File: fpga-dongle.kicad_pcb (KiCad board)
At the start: 2 copper layers, 85.8 x 137 mm, 109 parts, among them P1 USB_PWR, P2 PGM, P3 right, P4 left, P5 CONN_01X40, P6 CONN_01X40, P7 DBG_SWD, P8 USB_PWR, Q1 BC857, SW1 T1107A(6x3,8x2,5MM)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

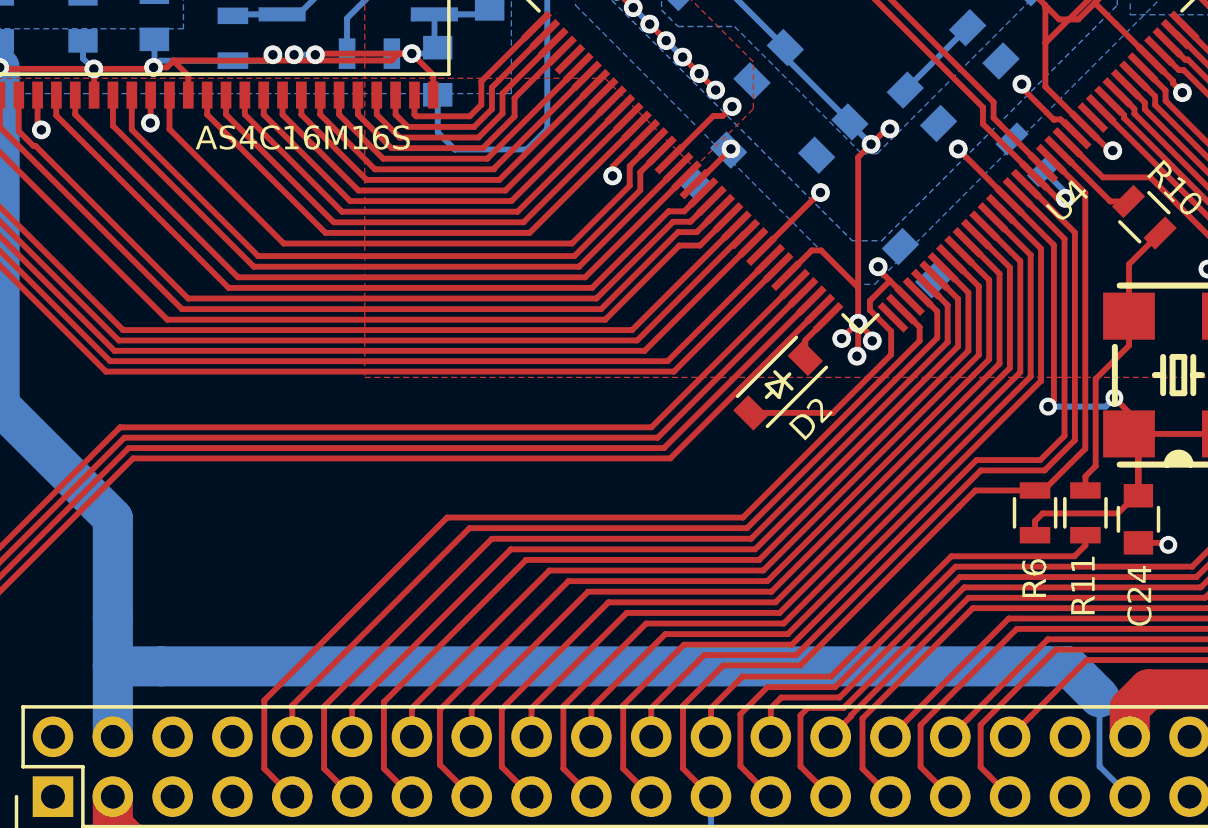
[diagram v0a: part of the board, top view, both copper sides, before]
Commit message: Fix 2V5 net diode from 1v2 to 3v3
Signed-off-by: Martin Ribelotta <martinribelotta@gmail.com>
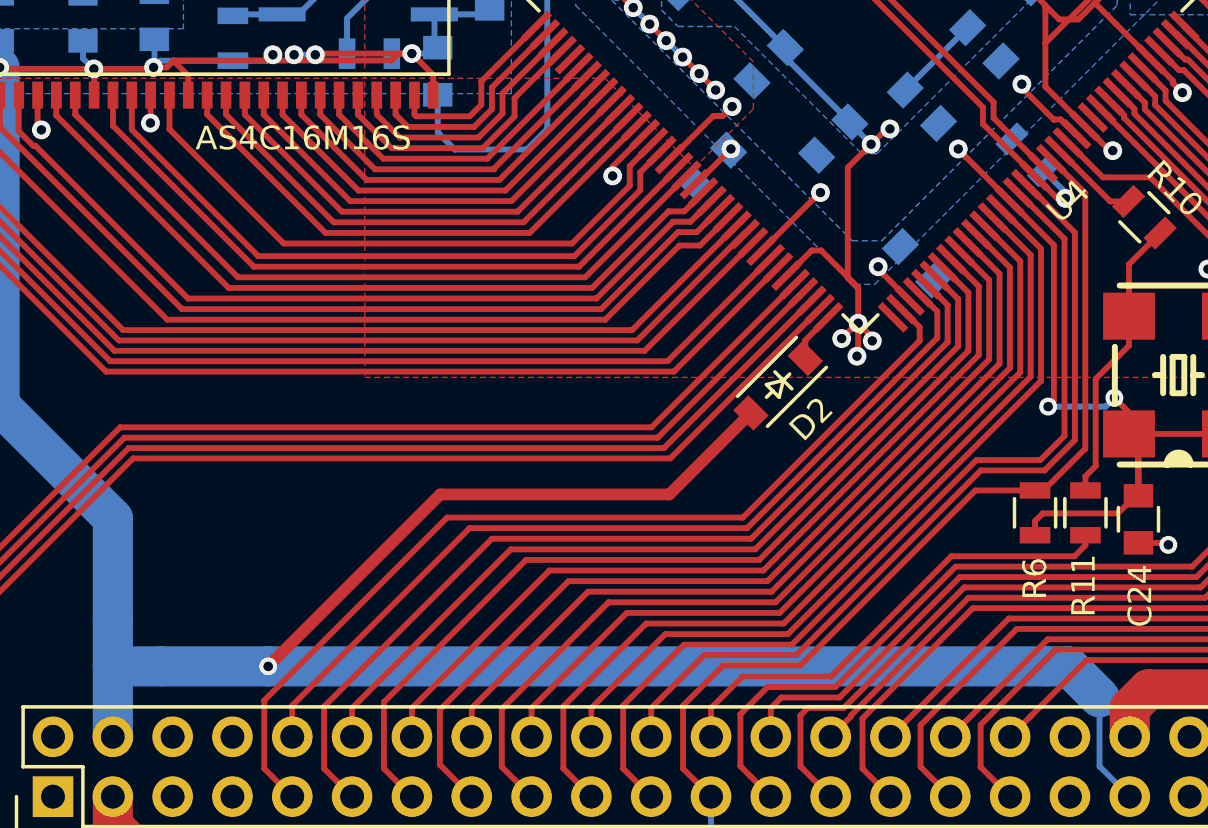
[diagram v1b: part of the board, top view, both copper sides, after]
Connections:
- D2 pad 2: +1V2 -> +3V3
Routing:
- net +3V3: track 528.2 -> 553.2 mm, vias 34 -> 35
- net +1V2: track 126.2 -> 115.3 mm
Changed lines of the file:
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@@
     (links 408)
     (no_connects 0)
-    (area 6.858 12.192 107.696001 163.068001)
+    (area 15.204999 17.544999 101.155001 154.695001)
     (thickness 1.6)
     (drawings 9)
@@
       (net 13 "Net-(D2-Pad1)"))
     (pad 2 smd rect (at 1.635 0 225) (size 0.91 1.22) (layers F.Cu F.Paste F.Mask)
-      (net 9 +1V2))
+      (net 1 +3V3))
   )
   (module OLIMEX_Devices-FP:FUSE-1206 (layer F.Cu)
@@
   (segment (start 81.802301 103.15) (end 81.743222 103.090921) (width 0.25) (layer B.Cu) (net 0))
   (via (at 81.743222 103.090921) (size 0.8) (drill 0.4) (layers F.Cu B.Cu) (net 0))
+  (segment (start 63.89388 124.90612) (end 60.43 128.37) (width 0.5) (layer F.Cu) (net 1))
+  (segment (start 60.43 128.37) (end 50.7 128.37) (width 0.5) (layer F.Cu) (net 1))
+  (segment (start 50.7 128.37) (end 43.4 135.67) (width 0.5) (layer F.Cu) (net 1))
+  (segment (start 76.46 135.67) (end 43.4 135.67) (width 1.7) (layer B.Cu) (net 1))
+  (segment (start 43.4 135.67) (end 38.862266 135.67) (width 1.7) (layer B.Cu) (net 1))
+  (via (at 43.4 135.67) (size 0.762) (drill 0.4064) (layers F.Cu B.Cu) (net 1))
   (segment (start 22.11 81) (end 22.11 79.215) (width 1.7) (layer B.Cu) (net 1))
   (segment (start 22.11 79.215) (end 23.05 78.275) (width 1.7) (layer B.Cu) (net 1))
@@
   (segment (start 78.7 139.917566) (end 78.7 136.99) (width 0.25) (layer B.Cu) (net 1))
   (segment (start 77.38 135.67) (end 76.46 135.67) (width 1.7) (layer B.Cu) (net 1))
-  (segment (start 76.46 135.67) (end 38.862266 135.67) (width 1.7) (layer B.Cu) (net 1))
   (segment (start 38.862266 135.67) (end 36.802266 135.67) (width 1.7) (layer B.Cu) (net 1))
   (segment (start 36.802266 135.67) (end 36.802266 138.659832) (width 1.7) (layer B.Cu) (net 1))
@@
   (segment (start 40.008666 110.588522) (end 39.365976 109.945832) (width 0.25) (layer F.Cu) (net 1))
   (segment (start 40.008666 111.413832) (end 40.008666 110.588522) (width 0.25) (layer F.Cu) (net 1) (status 10))
+  (segment (start 69 113.5) (end 68.01 114.49) (width 0.25) (layer F.Cu) (net 2))
+  (segment (start 68.01 114.49) (end 68.01 119.18) (width 0.25) (layer F.Cu) (net 2))
+  (segment (start 68.01 119.18) (end 68.45 119.62) (width 0.25) (layer F.Cu) (net 2))
   (segment (start 31.398213 48.16) (end 31.04 48.16) (width 0.25) (layer F.Cu) (net 2))
   (segment (start 32.108213 47.45) (end 31.398213 48.16) (width 0.25) (layer F.Cu) (net 2))
@@
   (segment (start 79.124071 113.77255) (end 79.260405 113.77255) (width 0.25) (layer F.Cu) (net 2))
   (via (at 79.260405 113.77255) (size 0.8) (drill 0.4) (layers F.Cu B.Cu) (net 2))
-  (segment (start 68.45 114.05) (end 68.45 119.62) (width 0.25) (layer F.Cu) (net 2))
   (segment (start 68.45 119.58) (end 68.45 119.62) (width 0.25) (layer F.Cu) (net 2))
   (segment (start 68.45 119.62) (end 68.45 121.1) (width 0.25) (layer F.Cu) (net 2))
@@
   (segment (start 69.65 112.85) (end 69 113.5) (width 0.25) (layer F.Cu) (net 2))
   (via (at 69.8 112.85) (size 0.8) (drill 0.4) (layers F.Cu B.Cu) (net 2))
-  (segment (start 69 113.5) (end 68.45 114.05) (width 0.25) (layer F.Cu) (net 2))
   (via (at 68.45 121.1) (size 0.8) (drill 0.4) (layers F.Cu B.Cu) (net 2))
   (segment (start 68.1 112.55) (end 68.1 112.6) (width 0.25) (layer B.Cu) (net 2) (status 30))
@@
   (segment (start 87.1 106.8) (end 81.05 106.8) (width 0.25) (layer B.Cu) (net 9))
   (segment (start 81.05 106.8) (end 71.95 97.7) (width 0.25) (layer B.Cu) (net 9))
-  (segment (start 68.949774 120.147947) (end 69.8 119.297721) (width 0.25) (layer F.Cu) (net 9))
-  (segment (start 63.89388 124.90612) (end 67.37924 124.90612) (width 0.25) (layer F.Cu) (net 9))
-  (segment (start 67.37924 124.90612) (end 69.85 122.43536) (width 0.25) (layer F.Cu) (net 9))
-  (segment (start 68.949774 120.541743) (end 68.949774 120.147947) (width 0.25) (layer F.Cu) (net 9))
-  (segment (start 69.85 121.441969) (end 68.949774 120.541743) (width 0.25) (layer F.Cu) (net 9))
-  (segment (start 69.85 122.43536) (end 69.85 121.441969) (width 0.25) (layer F.Cu) (net 9))
   (via (at 72.38 56.08) (size 0.762) (drill 0.4064) (layers F.Cu B.Cu) (net 9))
   (segment (start 72.38 55.3) (end 72.38 56.08) (width 1.2) (layer F.Cu) (net 9))

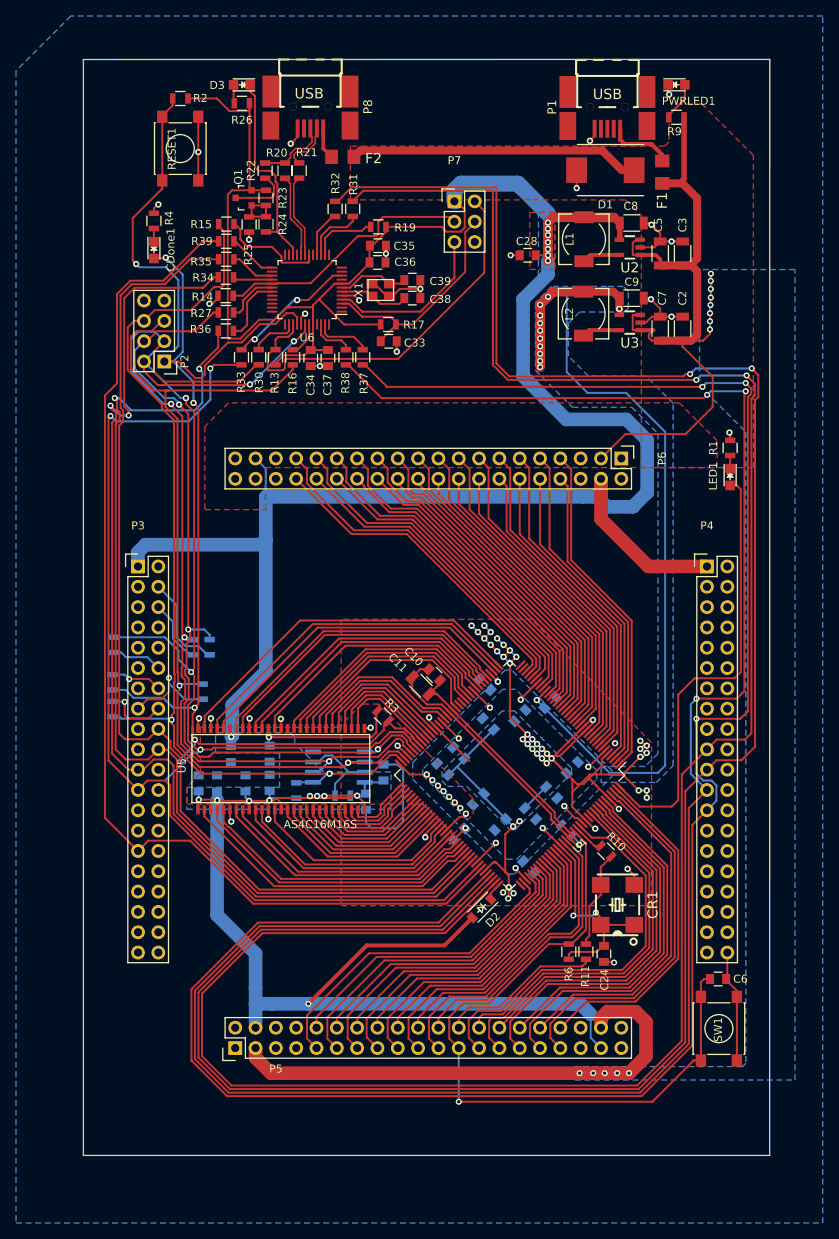
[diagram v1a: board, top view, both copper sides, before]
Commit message: Add miltiple power source handling, reroute pertinent nets
Signed-off-by: Martin Ribelotta <martinribelotta@gmail.com>
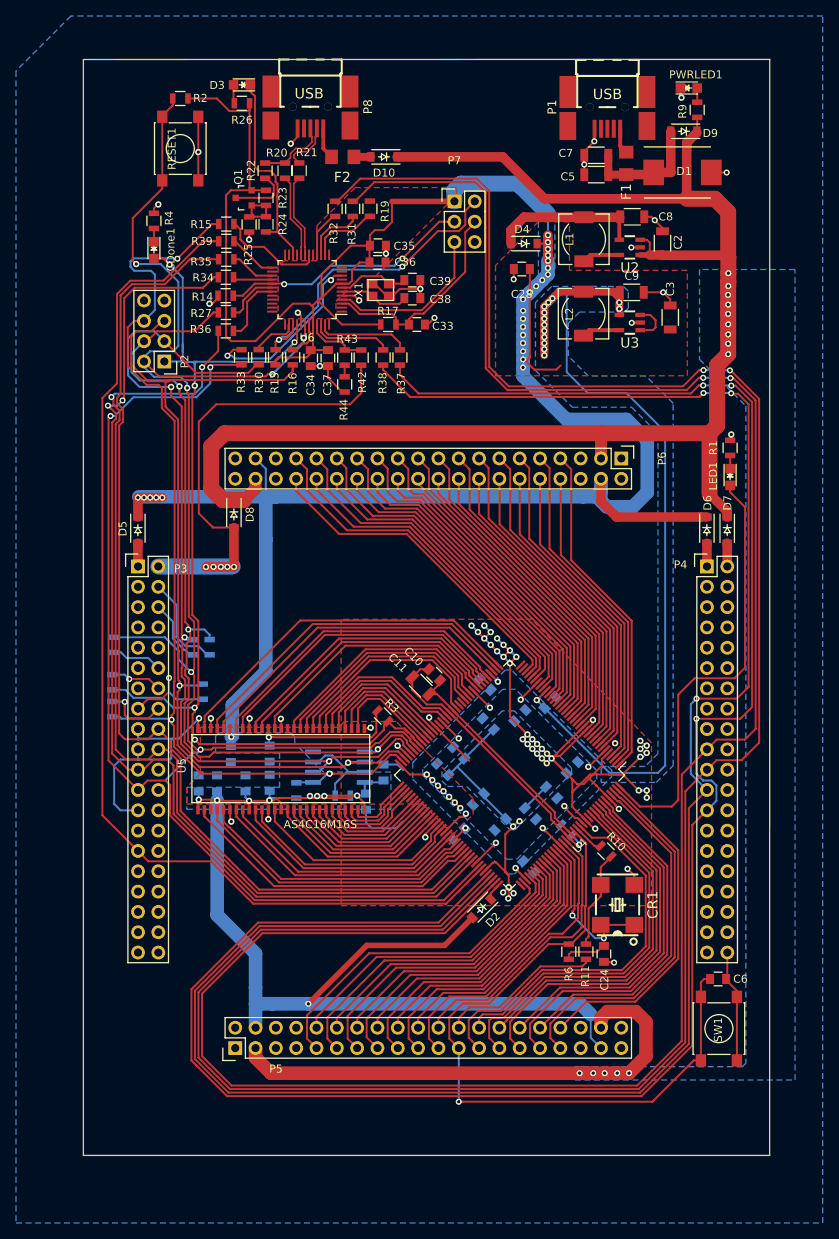
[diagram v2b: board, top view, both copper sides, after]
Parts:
- added D10: 1N5819(S4SOD-123), Diodes_SMD:SOD-123, F.Cu at (52.9, 29.8)
- added D4: 1N5819(S4SOD-123), Diodes_SMD:SOD-123, F.Cu at (70.4, 40.6)
- added D5: 1N5819(S4SOD-123), Diodes_SMD:SOD-123, F.Cu at (22.1, 76.5)
- added D6: 1N5819(S4SOD-123), Diodes_SMD:SOD-123, F.Cu at (93.2, 76.5)
- added D7: 1N5819(S4SOD-123), Diodes_SMD:SOD-123, F.Cu at (95.8, 76.5)
- added D8: 1N5819(S4SOD-123), Diodes_SMD:SOD-123, F.Cu at (34.1, 74.5)
- added D9: 1N5819(S4SOD-123), Diodes_SMD:SOD-123, F.Cu at (90.3, 26.6)
- added R42: 10k, Resistors_SMD:R_0805, F.Cu at (50.0, 54.9)
- added R43: 10k, Resistors_SMD:R_0805, F.Cu at (47.9, 54.9)
- added R44: 10k, Resistors_SMD:R_0805, F.Cu at (47.9, 58.2)
- moved C7 23.1 mm to (79.4, 29.6), turned to 0 degrees
- moved C5 12.7 mm to (79.4, 32.0), turned to 0 degrees
- moved C2 11.0 mm to (87.7, 40.6)
- moved D1 9.65 mm to (90.2, 31.8), turned to 0 degrees
- moved C3 8.14 mm to (88.6, 49.9)
- moved R37 4.65 mm to (54.9, 54.9)
- moved R38 4.65 mm to (52.8, 54.9)
- moved F1 4.63 mm to (83.1, 30.6)
- moved C33 4.09 mm to (57.0, 50.8)
- moved R9 2.76 mm to (92.0, 23.9), turned to 90 degrees
- moved R19 2.51 mm to (51.1, 36.3), turned to 90 degrees
- moved C28 1.87 mm to (70.1, 43.8)
- moved PWRLED1 1.59 mm to (91.0, 21.2)
- moved C8 0.78 mm to (83.9, 37.3)
- moved C9 0.73 mm to (83.8, 46.7)
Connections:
- C3 pad 2: +5V -> +3V3
- C5 pad 2: +5V -> Net-(C5-Pad2)
- C7 pad 2: +5V -> Net-(C5-Pad2)
- C8 pad 2: +3V3 -> Net-(C8-Pad2)
- D1 pad 1: +5V -> Net-(C5-Pad2)
- F1 pad 2: +5V -> Net-(C5-Pad2)
- F2 pad 2: +5V -> Net-(D10-Pad2)
- L1 pad 2: +3V3 -> Net-(C8-Pad2)
- P3 pad 1: +3V3 -> /CIAA_3V3_2
- P3 pad 2: (no net) -> /CIAA_5V2
- P4 pad 1: +3V3 -> /CIAA_3V3_1
- P4 pad 2: (no net) -> /CIAA_5V1
- U2 pad 4: +3V3 -> Net-(C8-Pad2)
- U3 pad 1: +5V -> +3V3
- U3 pad 3: +5V -> +3V3
- U6 pad 45: (no net) -> Net-(R42-Pad1)
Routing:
- net +5V: track 195.7 -> 262.9 mm, vias 13 -> 14
- net /CIAA_5V2: track 0.00 -> 59.7 mm, vias 0 -> 5
- net GND: track 254.9 -> 278.4 mm, vias 74 -> 75
- net +3V3: track 553.2 -> 573.5 mm, vias 35 -> 52
- net Net-(C8-Pad2): track 0.00 -> 18.6 mm
- net Net-(C5-Pad2): track 0.00 -> 15.5 mm
- net /DBG_SWDIO: track 50.1 -> 39.3 mm, vias 0 -> 2
- net Net-(R42-Pad1): track 0.00 -> 7.81 mm
- net /iCE40-CDONE: track 135.1 -> 127.5 mm, vias 4 -> 5
- net /P_SPI_SS: track 16.4 -> 22.8 mm
- net /RxD: track 258.5 -> 253.5 mm
- net Net-(F1-Pad1): track 8.18 -> 3.23 mm
- net /P_TxD: track 6.99 -> 11.7 mm
- net /iCE40-SS_B: track 120.7 -> 125.4 mm, vias 2 -> 3
- net /P_RxD: track 5.52 -> 10.0 mm
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- removed copper zone on F.Cu, net +5V
